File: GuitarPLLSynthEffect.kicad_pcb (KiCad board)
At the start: 2 copper layers, 183.6 x 110 mm, 57 parts

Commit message: Board Design Update RevA
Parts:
- removed C_RIP1: 100nF, Capacitors_SMD:CP_Elec_4x5.3
- added C_OABY1: 100nF, Capacitors_SMD:C_0805_HandSoldering, F.Cu at (150.7, 115.2)
- added C_OABY10: 100nF, Capacitors_SMD:C_0805_HandSoldering, F.Cu at (103.8, 8.64)
- added C_OABY11: 100nF, Capacitors_SMD:C_0805_HandSoldering, F.Cu at (120.4, 8.89)
- added C_OABY12: 100nF, Capacitors_SMD:C_0805_HandSoldering, F.Cu at (123.3, 19.1)
- added C_OABY13: 100nF, Capacitors_SMD:C_0805_HandSoldering, F.Cu at (61.0, 10.7)
- added C_OABY2: 100nF, Capacitors_SMD:C_0805_HandSoldering, F.Cu at (156.7, 124.7)
- added C_OABY3: 100nF, Capacitors_SMD:C_0805_HandSoldering, F.Cu at (8.26, 104.6)
- added C_OABY4: 100nF, Capacitors_SMD:C_0805_HandSoldering, F.Cu at (11.7, 115.2)
- added C_OABY5: 100nF, Capacitors_SMD:C_0805_HandSoldering, F.Cu at (-13.2, 135.0)
- added C_OABY6: 100nF, Capacitors_SMD:C_0805_HandSoldering, F.Cu at (-7.24, 144.5)
- added C_OABY7: 100nF, Capacitors_SMD:C_0805_HandSoldering, F.Cu at (37.0, 8.89)
- added C_OABY8: 100nF, Capacitors_SMD:C_0805_HandSoldering, F.Cu at (42.2, 20.2)
- added C_OABY9: 100nF, Capacitors_SMD:C_0805_HandSoldering, F.Cu at (93.6, 2.29)
- added C_PWRBY1: 10uF, Capacitors_SMD:C_0805_HandSoldering, F.Cu at (155.7, 150.1)
- added C_PWRBY2: 100nF, Capacitors_SMD:C_0805_HandSoldering, F.Cu at (155.7, 148.2)
- added C_PWRBY3: 100nF, Capacitors_SMD:C_0805_HandSoldering, F.Cu at (3.94, 40.6)
- added J_AUX2MAIN_LED1: Conn_01x04, Pin_Headers:Pin_Header_Straight_1x04_Pitch2.54mm, F.Cu at (144.8, 99.1)
- added J_MAIN2AUX_LED1: Conn_01x04, Pin_Headers:Pin_Header_Straight_1x04_Pitch2.54mm, F.Cu at (45.7, 99.1)
- added R_LED1: 2K7, Resistors_SMD:R_0805_HandSoldering, F.Cu at (177.3, 100.1)
- R_MIX_F1: moved to B.Cu
- moved U_OA_FXVOL1 272.3 mm to (-10.9, 140.1)
- moved U_OA_MIX1 251.0 mm to (7.73, 109.8)
- moved R_OA_OUT_F1 242.9 mm to (-9.40, 146.9), turned to 270 degrees
- moved R_MIX_G1 238.4 mm to (5.08, 115.2)
- moved U_NEG2 236.2 mm to (4.57, 45.6)
- moved C2_NEG2 232.4 mm to (3.56, 52.6)
- moved R_OA_IN1 226.8 mm to (37.0, 20.2)
- moved U_OAFX_IN1 226.4 mm to (39.0, 14.6)
- moved R_MIX_F1 221.1 mm to (9.14, 109.7), turned to 180 degrees
- moved C1_NEG2 213.0 mm to (10.3, 45.0), turned to 90 degrees
- moved C_SAW1 198.3 mm to (98.6, -0.13)
- moved C_VCO1 195.7 mm to (72.0, 19.8)
- moved R_FXVOL1 193.2 mm to (-12.6, 146.9), turned to 270 degrees
- moved C_SUSTAIN1 190.1 mm to (41.7, 8.89)
- moved C_HOLD2 189.1 mm to (85.6, 24.6), turned to 180 degrees
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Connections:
- D_ON1 pad 1: /GND -> Net-(D_ON1-Pad1)
- SW_BYPASS1 pad 9: Net-(D_ON1-Pad2) -> /LED_ANODE
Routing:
- net Net-(J_DIRTY_IN1-Pad1): track 0.00 -> 55.0 mm
- net /GND: track 0.00 -> 52.9 mm, vias 0 -> 24
- net /9V: track 0.00 -> 31.4 mm
- net /Sheet5AC1BF71/-9V: track 0.00 -> 10.1 mm
- net /-9V: track 0.00 -> 10.1 mm
- net Net-(C_SAW1-Pad2): track 0.00 -> 10.0 mm
- net /MIX_P3: track 0.00 -> 6.88 mm
- net Net-(R_SAW1-Pad1): track 0.00 -> 6.60 mm
- net /Sheet5AC1BF71/DAMP_P1_2: track 0.00 -> 6.39 mm
- net Net-(R_MIX_F1-Pad2): track 0.00 -> 5.92 mm, vias 0 -> 1
- net Net-(SW_BYPASS1-Pad1): track 0.00 -> 5.50 mm
- net Net-(C2_NEG2-Pad1): track 0.00 -> 4.71 mm
- net Net-(J_OU1-Pad1): track 0.00 -> 4.58 mm, vias 0 -> 1
- net Net-(C2_NEG1-Pad1): track 0.00 -> 4.46 mm
- net Net-(C2_NEG1-Pad2): track 0.00 -> 4.36 mm
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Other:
- board size 183.6 x 110 mm -> 183.9 x 110 mm

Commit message: Completed First Draft board Layout RevA
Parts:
- C_OABY8, R_SAW2: moved to B.Cu
- moved C_OABY5 117.7 mm to (102.6, 114.3), turned to 0 degrees
- moved R_FXVOL1 116.3 mm to (97.8, 110.2), turned to 0 degrees
- moved U_NEG1 114.1 mm to (50.7, 119.9)
- moved C1_NEG1 114.1 mm to (56.4, 119.4)
- moved D_IN1 113.8 mm to (45.7, 116.8)
- moved C_PWRBY2 113.6 mm to (45.7, 119.9)
- moved C_PWRBY1 113.3 mm to (45.7, 122.9)
- moved U_OA_FXVOL1 109.9 mm to (96.1, 115.1), turned to 270 degrees
- moved C2_NEG1 106.7 mm to (61.5, 119.4), turned to 90 degrees
- moved R_OA_OUT_F1 103.2 mm to (89.3, 116.6), turned to 180 degrees
- moved C_OABY6 102.3 mm to (91.7, 118.6), turned to 180 degrees
- moved C_OABY11 89.1 mm to (108.3, 97.2), turned to 180 degrees
- moved C_SAW1 78.1 mm to (97.9, 78.0), turned to 180 degrees
- moved U_OAFX_OUT1 77.9 mm to (108.9, 91.6), turned to 180 degrees
- moved C_OABY13 77.5 mm to (73.4, 87.1), turned to 270 degrees
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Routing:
- net /9V: track 31.4 -> 344.7 mm, vias 0 -> 10
- net /MIX_P2: track 0.00 -> 110.4 mm
- net /Sheet5AC1BF71/-9V: track 10.1 -> 113.5 mm, vias 0 -> 3
- net /LED_ANODE: track 0.00 -> 92.5 mm
- net /INSW_P1: track 2.42 -> 92.4 mm, vias 0 -> 2
- net /Sheet5AC1BF71/DAMP_P3: track 0.00 -> 85.6 mm
- net /INSW_P3: track 0.00 -> 80.0 mm
- net /Sheet5AC1BF71/VCORETURN: track 1.27 -> 75.7 mm, vias 0 -> 2
- net /Sheet5AC1BF71/SWING_P3: track 0.00 -> 67.0 mm, vias 0 -> 1
- net /-9V: track 10.1 -> 75.4 mm, vias 0 -> 4
- net Net-(R_OA_OUT1-Pad1): track 2.72 -> 67.7 mm
- net /Sheet5AC1BF71/SIG_OUT: track 2.70 -> 63.0 mm
- net /MIX_P3: track 6.88 -> 65.5 mm
- net /Sheet5AC1BF71/HOLDSEL_P3: track 0.00 -> 52.4 mm
- net Net-(J_AUX2MAIN_FXSW1-Pad3): track 0.00 -> 51.1 mm
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- added copper zone on B.Cu, net /GND

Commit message: Second draft PCB layout
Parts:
- removed C_SAW1: 10nF, Capacitors_SMD:C_0805_HandSoldering
- removed R_SAW2: 1K, Resistors_SMD:R_0805_HandSoldering
- added C_SAWINT1: 10nF, Capacitors_SMD:C_0805_HandSoldering, F.Cu at (112.4, 142.4)
- added R_SAWFB1: 1K, Resistors_SMD:R_0805_HandSoldering, F.Cu at (114.4, 131.4)
- added R_SAWJOIN1: 10R, Resistors_SMD:R_0805_HandSoldering, F.Cu at (107.6, 139.3)
- added R_SWING1: 22K, Resistors_SMD:R_0805_HandSoldering, F.Cu at (89.5, 135.6)
- C_PWRBY1: footprint Capacitors_SMD:C_0805_HandSoldering -> Capacitors_SMD:CP_Elec_4x5.3
- R_MIX_F1: moved to F.Cu
- moved FXVOL1 84.2 mm to (97.7, 78.4)
- moved R_LED1 84.2 mm to (93.1, 102.2)
- moved SW_INSW1 84.2 mm to (69.7, 97.2)
- moved DAMPEN1 84.2 mm to (128.7, 57.0)
- moved D_ON1 84.2 mm to (101.7, 103.8)
- moved J_AUX2MAIN_FX1 84.2 mm to (60.6, 58.5)
- moved J_AUX2MAIN_FXSW1 84.2 mm to (140.3, 90.0)
- moved J_AUX2MAIN_INSW1 84.2 mm to (60.6, 76.3)
- moved J_AUX2MAIN_LED1 84.2 mm to (60.6, 101.2)
- moved J_AUX2MAIN_PLL1 84.2 mm to (140.3, 66.2)
- moved J_AUX2MAIN_VOL1 84.2 mm to (140.3, 72.3)
- moved MIX1 84.2 mm to (128.7, 78.4)
- moved SWING1 84.2 mm to (97.5, 57.0)
- moved SW_HOLD1 84.2 mm to (131.2, 97.2)
- moved SW_WAVE1 84.2 mm to (100.2, 97.2)
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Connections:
- C_PWRBY1 pad 1: Net-(C_PWRBY1-Pad1) -> /9V
- C_PWRBY2 pad 2: Net-(C_PWRBY1-Pad1) -> /9V
- D_IN1 pad 2: Net-(C_PWRBY1-Pad1) -> Net-(D_IN1-Pad2)
- J_POWER1 pad 2: Net-(C_PWRBY1-Pad1) -> Net-(D_IN1-Pad2)
- U_PLL1 pad 13: /Sheet5AC1BF71/SWING_P3 -> Net-(R_SWING1-Pad2)
- U_SAW_OA1 pad 1: Net-(C_SAW1-Pad2) -> Net-(R_SAWFB1-Pad1)
- U_SAW_OA1 pad 6: Net-(C_SAW1-Pad2) -> Net-(C_SAWINT1-Pad2)
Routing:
- net /9V: track 344.7 -> 325.8 mm
- net Net-(C_PWRBY1-Pad1): track 16.6 -> 0.00 mm
- net Net-(C_SAW1-Pad2): track 12.9 -> 0.00 mm, vias 1 -> 0
- net Net-(R_SAWFB1-Pad1): track 0.00 -> 12.6 mm
- net Net-(D_IN1-Pad2): track 0.00 -> 11.9 mm
- net /Sheet5AC1BF71/SWING_P3: track 67.0 -> 55.5 mm, vias 1 -> 2
- net Net-(J_OU1-Pad1): track 45.1 -> 33.7 mm, vias 1 -> 2
- net /LED_ANODE: track 92.5 -> 81.5 mm
- net Net-(C2_NEG1-Pad2): track 12.6 -> 23.6 mm
- net /INSW_P3: track 80.0 -> 70.8 mm
- net Net-(C2_NEG1-Pad1): track 13.7 -> 22.6 mm
- net Net-(R_SWING1-Pad2): track 0.00 -> 8.69 mm
- net /GND: track 57.7 -> 49.6 mm, vias 23 -> 25
- net /-9V: track 75.4 -> 82.8 mm, vias 4 -> 2
- net Net-(C_SAWINT1-Pad2): track 0.00 -> 7.29 mm
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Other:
- board size 183.9 x 110 mm -> 85.1 x 164.1 mm

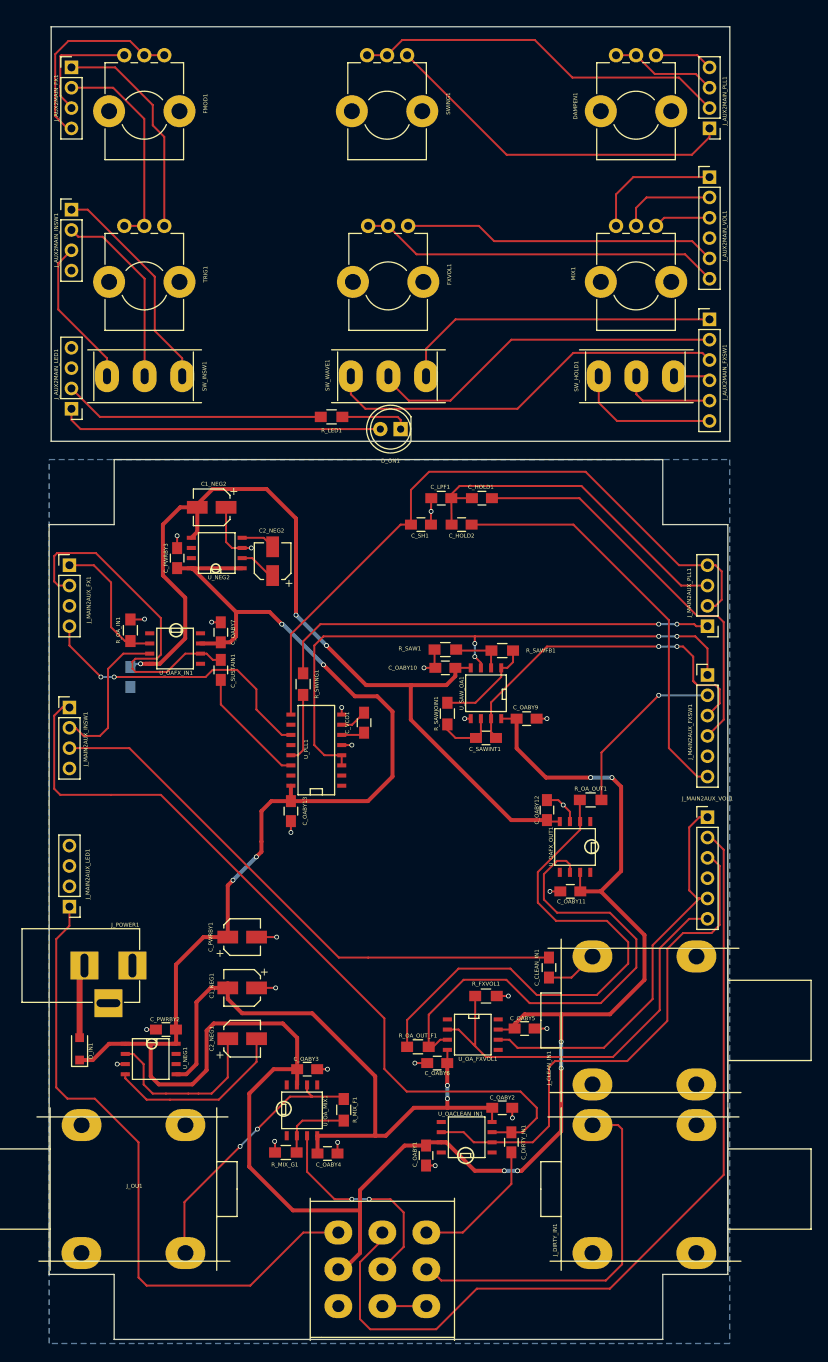
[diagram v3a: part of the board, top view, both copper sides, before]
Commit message: Corrections to board dimensions, adjusted layout to fit
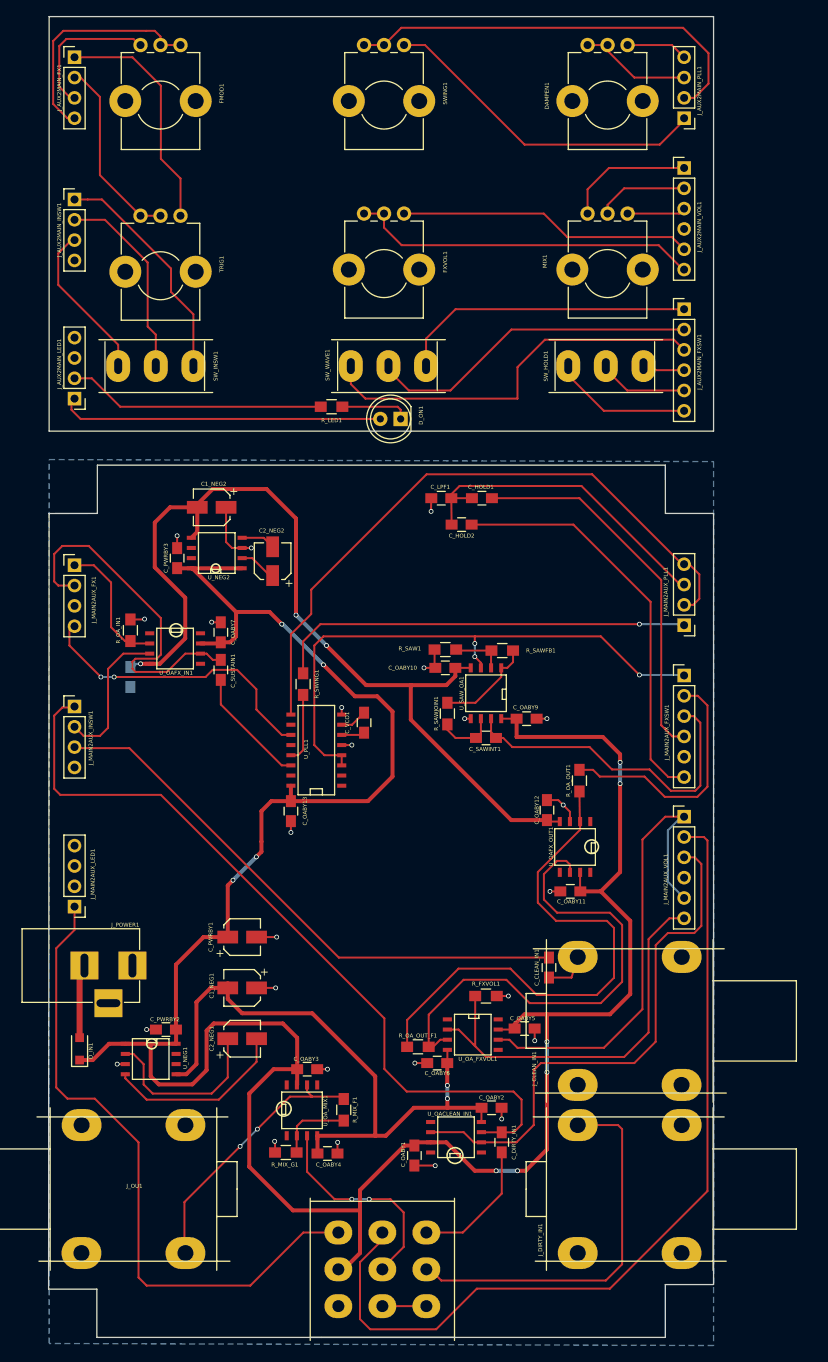
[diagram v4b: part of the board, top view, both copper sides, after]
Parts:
- removed C_SH1: 100nF, Capacitors_SMD:C_0805_HandSoldering
- moved SW_HOLD1 4.02 mm to (127.4, 95.9)
- moved MIX1 3.88 mm to (125.1, 76.8)
- moved DAMPEN1 3.78 mm to (125.1, 55.8)
- moved J_AUX2MAIN_FXSW1 3.42 mm to (137.2, 88.8)
- moved J_AUX2MAIN_PLL1 3.42 mm to (137.2, 64.9)
- moved J_AUX2MAIN_VOL1 3.37 mm to (137.2, 71.1)
- moved J_MAIN2AUX_PLL1 2.92 mm to (137.2, 128.3)
- moved J_MAIN2AUX_FXSW1 2.92 mm to (137.2, 134.6)
- moved J_MAIN2AUX_VOL1 2.92 mm to (137.2, 152.2)
- moved R_OA_OUT1 2.79 mm to (124.1, 147.7), turned to 90 degrees
- moved FMOD1 2.39 mm to (69.2, 55.8)
- moved TRIG1 2.39 mm to (69.2, 77.1)
- moved SW_INSW1 1.89 mm to (71.1, 95.9)
- moved J_CLEAN_IN1 1.84 mm to (130.4, 177.7)
- moved J_DIRTY_IN1 1.84 mm to (130.4, 198.8)
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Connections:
- J_AUX2MAIN_INSW1 pad 4: Net-(J_AUX2MAIN_INSW1-Pad4) -> (no net)
- J_AUX2MAIN_LED1 pad 3: Net-(J_AUX2MAIN_LED1-Pad3) -> (no net)
- J_AUX2MAIN_LED1 pad 4: Net-(J_AUX2MAIN_LED1-Pad4) -> (no net)
- J_AUX2MAIN_VOL1 pad 4: Net-(J_AUX2MAIN_VOL1-Pad4) -> (no net)
- J_CLEAN_IN1 pad 3: Net-(J_CLEAN_IN1-Pad3) -> (no net)
- J_DIRTY_IN1 pad 3: Net-(J_DIRTY_IN1-Pad3) -> (no net)
- J_MAIN2AUX_INSW1 pad 4: Net-(J_MAIN2AUX_INSW1-Pad4) -> (no net)
- J_MAIN2AUX_LED1 pad 3: Net-(J_MAIN2AUX_LED1-Pad3) -> (no net)
- J_MAIN2AUX_LED1 pad 4: Net-(J_MAIN2AUX_LED1-Pad4) -> (no net)
- J_MAIN2AUX_VOL1 pad 4: Net-(J_MAIN2AUX_VOL1-Pad4) -> (no net)
- J_OU1 pad 2: Net-(J_OU1-Pad2) -> (no net)
- J_OU1 pad 3: Net-(J_OU1-Pad3) -> (no net)
- J_POWER1 pad 3: Net-(J_POWER1-Pad3) -> (no net)
- SW_BYPASS1 pad 7: Net-(SW_BYPASS1-Pad7) -> (no net)
- U_NEG1 pad 6: Net-(U_NEG1-Pad6) -> (no net)
- U_NEG1 pad 7: Net-(U_NEG1-Pad7) -> (no net)
- U_NEG2 pad 6: Net-(U_NEG2-Pad6) -> (no net)
- U_NEG2 pad 7: Net-(U_NEG2-Pad7) -> (no net)
- U_OACLEAN_IN1 pad 1: Net-(U_OACLEAN_IN1-Pad1) -> (no net)
- U_OACLEAN_IN1 pad 5: Net-(U_OACLEAN_IN1-Pad5) -> (no net)
- U_OACLEAN_IN1 pad 8: Net-(U_OACLEAN_IN1-Pad8) -> (no net)
- U_OAFX_IN1 pad 1: Net-(U_OAFX_IN1-Pad1) -> (no net)
- U_OAFX_IN1 pad 5: Net-(U_OAFX_IN1-Pad5) -> (no net)
- U_OAFX_IN1 pad 8: Net-(U_OAFX_IN1-Pad8) -> (no net)
- U_OAFX_OUT1 pad 1: Net-(U_OAFX_OUT1-Pad1) -> (no net)
- U_OAFX_OUT1 pad 5: Net-(U_OAFX_OUT1-Pad5) -> (no net)
- U_OAFX_OUT1 pad 8: Net-(U_OAFX_OUT1-Pad8) -> (no net)
- U_OA_FXVOL1 pad 1: Net-(U_OA_FXVOL1-Pad1) -> (no net)
- U_OA_FXVOL1 pad 5: Net-(U_OA_FXVOL1-Pad5) -> (no net)
- U_OA_FXVOL1 pad 8: Net-(U_OA_FXVOL1-Pad8) -> (no net)
- U_OA_MIX1 pad 1: Net-(U_OA_MIX1-Pad1) -> (no net)
- U_OA_MIX1 pad 5: Net-(U_OA_MIX1-Pad5) -> (no net)
- U_OA_MIX1 pad 8: Net-(U_OA_MIX1-Pad8) -> (no net)
- U_PLL1 pad 1: Net-(U_PLL1-Pad1) -> (no net)
- U_PLL1 pad 10: Net-(U_PLL1-Pad10) -> (no net)
- U_PLL1 pad 12: Net-(U_PLL1-Pad12) -> (no net)
- U_PLL1 pad 15: Net-(U_PLL1-Pad15) -> (no net)
- U_PLL1 pad 2: Net-(U_PLL1-Pad2) -> (no net)
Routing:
- net /Sheet5AC1BF71/WAVESEL_P2: track 22.1 -> 31.5 mm, vias 1 -> 0
- net /FXVOL_P3: track 50.9 -> 60.1 mm
- net Net-(J_AUX2MAIN_PLL1-Pad2): track 47.1 -> 52.9 mm
- net /Sheet5AC1BF71/VCORETURN: track 75.5 -> 70.7 mm, vias 4 -> 3
- net /Sheet5AC1BF71/HOLDSEL_P1: track 50.5 -> 47.0 mm
- net Net-(FMOD1-Pad1): track 15.1 -> 18.5 mm
- net /Sheet5AC1BF71/DAMP_P1_2: track 44.0 -> 40.7 mm
- net Net-(J_AUX2MAIN_PLL1-Pad1): track 45.0 -> 41.7 mm
- net Net-(FMOD1-Pad2): track 25.5 -> 28.7 mm
- net Net-(J_AUX2MAIN_FXSW1-Pad2): track 44.8 -> 41.7 mm
- net Net-(J_AUX2MAIN_FXSW1-Pad1): track 40.4 -> 37.2 mm
- net /Sheet5AC1BF71/WAVESEL_P3: track 44.5 -> 41.5 mm, vias 2 -> 0
- net Net-(J_AUX2MAIN_FX1-Pad2): track 26.6 -> 23.6 mm
- net /Sheet5AC1BF71/DAMP_P3: track 85.6 -> 82.8 mm
- net /Sheet5AC1BF71/SWING_P3: track 55.5 -> 52.7 mm, vias 2 -> 1
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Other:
- board size 85.1 x 164.1 mm -> 83.1 x 165.1 mm

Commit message: final layout
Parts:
- C_OABY8: moved to F.Cu
- moved C_CLEAN_IN1 17.7 mm to (106.0, 160.5), turned to 180 degrees
- moved R_OA_OUT_F1 11.4 mm to (100.3, 170.2)
- moved C_OABY5 6.65 mm to (114.3, 172.7), turned to 90 degrees
- moved R_FXVOL1 6.10 mm to (109.2, 169.4)
- moved U_OA_FXVOL1 5.84 mm to (106.7, 175.3)
- moved C_HOLD2 4.83 mm to (109.3, 120.5)
- moved C_LPF1 4.58 mm to (106.6, 117.0)
- moved C_HOLD1 4.57 mm to (112.0, 117.0)
- moved D_IN1 4.30 mm to (63.0, 185.3), turned to 180 degrees
- moved J_POWER1 2.17 mm to (67.9, 173.0)
- moved SW_BYPASS1 0.46 mm to (99.6, 208.3)
- moved J_MAIN2AUX_INSW1 0.13 mm to (61.0, 138.6)
- moved J_MAIN2AUX_PLL1 0.06 mm to (137.2, 128.3)
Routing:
- net /INSW_P3: track 70.8 -> 51.9 mm
- net Net-(J_DIRTY_IN1-Pad1): track 48.5 -> 32.2 mm
- net Net-(C_CLEAN_IN1-Pad1): track 5.51 -> 21.3 mm
- net /Sheet5AC1BF71/SIG_OUT: track 61.5 -> 72.4 mm
- net Net-(R_OA_OUT1-Pad1): track 67.3 -> 77.6 mm
- net /GND: track 49.4 -> 57.0 mm, vias 25 -> 26
- net /FXVOL_P3: track 60.1 -> 67.3 mm
- net /9V: track 325.3 -> 332.1 mm
- net /FXVOL_P1_2: track 51.6 -> 57.7 mm
- net /-9V: track 81.5 -> 87.3 mm
- net Net-(C_SUSTAIN1-Pad2): track 15.0 -> 17.8 mm
- net /Sheet5AC1BF71/HOLDSEL_P1: track 47.0 -> 44.2 mm
- net /Sheet5AC1BF71/HOLDSEL_P3: track 52.0 -> 50.1 mm
- net /Sheet5AC1BF71/DAMP_P3: track 82.8 -> 81.3 mm
- net /Sheet5AC1BF71/DAMP_P1_2: track 40.7 -> 41.9 mm
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
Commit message: Layout design corrections
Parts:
- moved C_PWRBY1 13.1 mm to (92.8, 174.5), turned to 270 degrees
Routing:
- net /9V: track 332.1 -> 340.0 mm
- net /INSW_P1: track 97.9 -> 102.4 mm
- net /Sheet5AC1BF71/-9V: track 116.9 -> 114.1 mm
- net /FXVOL_P3: track 67.3 -> 64.7 mm
- net /FXVOL_P1_2: track 57.7 -> 55.2 mm
- net Net-(J_OU1-Pad1): track 33.7 -> 35.6 mm
- net /GND: track 57.0 -> 57.9 mm

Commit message: layout updates
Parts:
- moved FMOD1 55.9 mm to (125.1, 56.5)
- moved DAMPEN1 27.9 mm to (97.2, 56.5)
- moved SWING1 27.9 mm to (69.2, 56.5)
- moved D_ON1 12.8 mm to (88.9, 102.2)
- moved R_LED1 11.2 mm to (81.9, 101.0)
- moved C2_NEG2 8.83 mm to (86.1, 111.4), turned to 180 degrees
- moved SW_INSW1 3.86 mm to (71.8, 99.7)
- moved SW_WAVE1 3.84 mm to (99.7, 99.7)
- moved SW_HOLD1 3.82 mm to (127.6, 99.7)
- moved C1_NEG2 2.10 mm to (78.0, 111.4)
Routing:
- net Net-(FMOD1-Pad2): track 28.7 -> 85.9 mm
- net Net-(FMOD1-Pad1): track 18.5 -> 75.2 mm
- net Net-(J_AUX2MAIN_PLL1-Pad2): track 52.9 -> 83.2 mm
- net Net-(DAMPEN1-Pad3): track 7.70 -> 36.3 mm
- net Net-(DAMPEN1-Pad1): track 14.2 -> 42.1 mm
- net Net-(J_AUX2MAIN_PLL1-Pad1): track 41.7 -> 68.7 mm
- net /Sheet5AC1BF71/-9V: track 114.1 -> 138.1 mm
- net Net-(D_ON1-Pad2): track 40.5 -> 28.7 mm
- net Net-(C2_NEG2-Pad1): track 4.71 -> 13.1 mm
- net Net-(J_AUX2MAIN_LED1-Pad2): track 32.3 -> 25.7 mm
- net Net-(J_AUX2MAIN_INSW1-Pad2): track 24.7 -> 29.2 mm
- net Net-(J_AUX2MAIN_INSW1-Pad1): track 29.4 -> 33.0 mm
- net Net-(J_AUX2MAIN_INSW1-Pad3): track 19.5 -> 22.9 mm
- net Net-(J_AUX2MAIN_FXSW1-Pad4): track 6.01 -> 8.82 mm
- net Net-(J_AUX2MAIN_FXSW1-Pad2): track 41.7 -> 44.4 mm
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
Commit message: layout update
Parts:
- removed C_OABY10, C_OABY11, C_OABY12, C_OABY5, C_OABY6, C_OABY7, C_OABY8, C_OABY9: 100nF, Capacitors_SMD:C_0805_HandSoldering
- removed U_OACLEAN_IN1, U_OAFX_IN1, U_OAFX_OUT1, U_OA_FXVOL1, U_OA_MIX1: _TL071, SMD_Packages:SOIC-8-N
- removed U_SAW_OA1: _TL072, SMD_Packages:SOIC-8-N
- added U_MAINOA1: TL074, SMD_Packages:SOIC-14_N, F.Cu at (99.7, 189.2)
- added U_OAFX1: TL074, SMD_Packages:SOIC-14_N, F.Cu at (97.7, 145.5)
- C_OABY1, C_OABY13, C_OABY2, C_OABY3, C_OABY4, C_PWRBY3: moved to B.Cu
- moved C_OABY4 49.7 mm to (96.4, 144.8), turned to 180 degrees
- moved C_OABY3 37.7 mm to (96.4, 146.6), turned to 180 degrees
- moved R_OA_IN1 30.6 mm to (97.0, 138.4), turned to 180 degrees
- moved C_OABY13 29.4 mm to (90.8, 122.2)
- moved R_SWING1 29.2 mm to (108.0, 113.0)
- moved C_SUSTAIN1 27.1 mm to (96.5, 113.0)
- moved R_SAW1 24.9 mm to (107.3, 156.2), turned to 0 degrees
- moved C_HOLD2 22.0 mm to (130.9, 124.5), turned to 270 degrees
- moved R_SAWFB1 21.5 mm to (107.3, 151.8)
- moved U_PLL1 21.0 mm to (98.2, 124.1), turned to 0 degrees
- moved R_OA_OUT1 20.8 mm to (107.3, 160.0), turned to 0 degrees
- moved R_FXVOL1 19.8 mm to (92.8, 180.6), turned to 180 degrees
- moved C_HOLD1 16.9 mm to (127.1, 124.5), turned to 270 degrees
- moved R_MIX_F1 16.2 mm to (84.2, 201.3)
- moved C_OABY2 14.9 mm to (98.3, 190.0), turned to 180 degrees
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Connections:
- C_OABY4 pad 1: /-9V -> /Sheet5AC1BF71/-9V
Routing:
- net /Sheet5AC1BF71/-9V: track 138.1 -> 50.1 mm, vias 2 -> 3
- net /9V: track 340.0 -> 267.4 mm, vias 10 -> 9
- net Net-(R_OA_OUT1-Pad1): track 77.6 -> 22.9 mm
- net /INSW_P1: track 102.4 -> 151.3 mm, vias 0 -> 2
- net /Sheet5AC1BF71/TRIG_P3: track 17.4 -> 62.4 mm
- net /Sheet5AC1BF71/WAVESEL_P2: track 31.3 -> 73.8 mm
- net /Sheet5AC1BF71/TRIG_P1_2: track 44.9 -> 84.8 mm, vias 4 -> 0
- net /-9V: track 87.5 -> 52.2 mm, vias 2 -> 1
- net /GND: track 58.4 -> 27.6 mm, vias 26 -> 15
- net /Sheet5AC1BF71/FMOD_P2_P3: track 38.0 -> 66.4 mm, vias 4 -> 0
- net /Sheet5AC1BF71/DAMP_P3: track 79.5 -> 51.6 mm
- net /INSW_P2: track 19.0 -> 39.5 mm
- net /Sheet5AC1BF71/HOLDSEL_P3: track 50.1 -> 31.5 mm
- net /Sheet5AC1BF71/HOLDSEL_P1: track 44.2 -> 27.1 mm
- net /MIX_P2: track 110.6 -> 95.5 mm
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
